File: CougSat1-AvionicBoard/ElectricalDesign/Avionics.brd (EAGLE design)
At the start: 90.4 x 95.8 mm, 213 parts, among them J1 +X Panel GPS, J10 iFJR SD1, J11 -Y, J12 +Z, J13 +X, J14 -Z, J15 +Y, J16 IFJR SD0, J2 IHU SD1, J3 SWD, J4 CougSat Card, J5 -X, J6 IHU SD0, J8 SWD, J9 SWD, U1 STM32L476RGT, U10 BNO055, U11 M24M01, U12 TXS0102DQM, U13 TXS0102DQM, U14 AD8515, U15 BNO055, U16 BNO055, U17 TXS0102DQM, U18 TXS0102DQM, U19 AD8515, U2 STM32L476RGT, U20 INA199C2, U21 INA199C2, U22 TXS0102DQM, U23 TXS0102DQM, U24 AD8515, U25 AD7291, U26 AD7291, U27 TXS0102DQM, U28 INA199C2, U29 AD8515, U3 STM32L476RGT, U30 DRV8837, U4 M24M01, U5 TXS0102DQM, U6 DRV8837, U7 DRV8837, U8 AD7291, U9 Venus838FLPx-L, Y1 8MHz ±10ppm, Y10 32.768kHz ±10ppm, Y2 32.768kHz ±10ppm, Y3 8MHz ±10ppm, Y4 32.768kHz ±10ppm, Y5 8MHz ±10ppm, Y6 32.768kHz ±10ppm, Y7 32.768kHz ±10ppm, Y8 32.768kHz ±10ppm

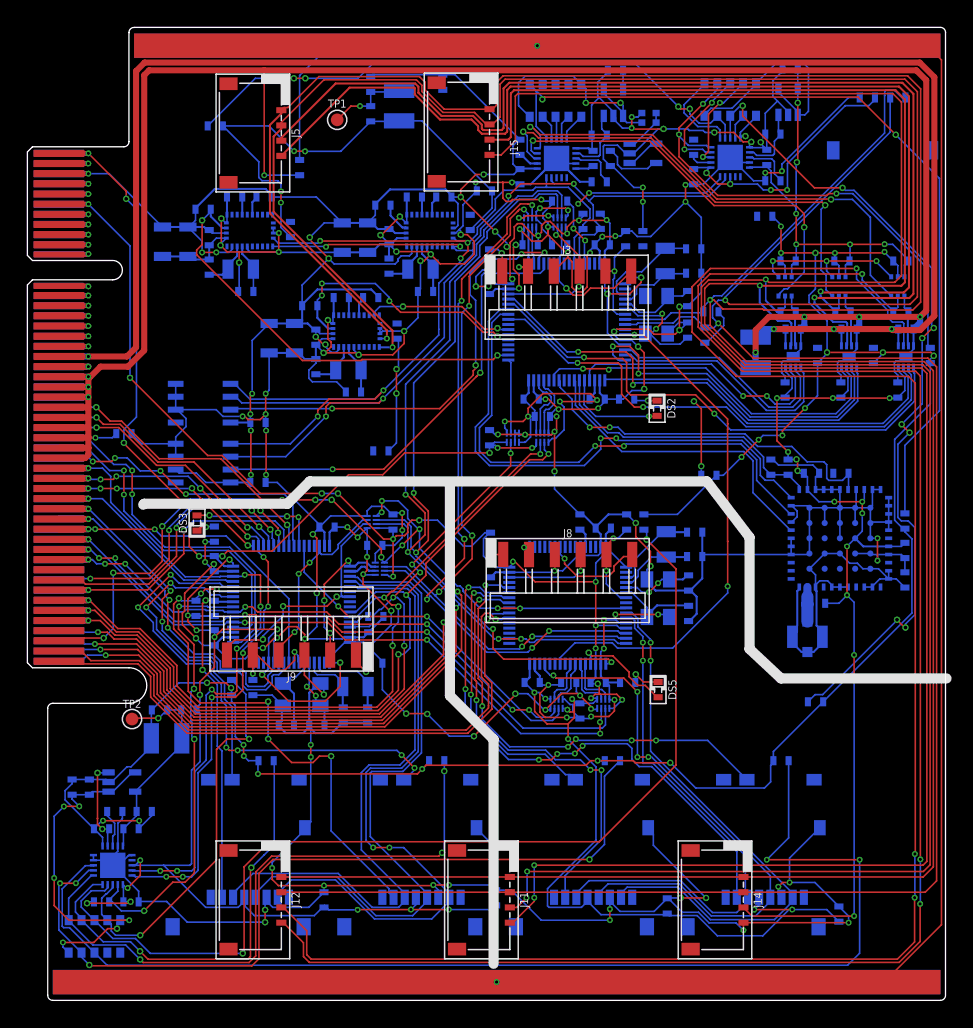
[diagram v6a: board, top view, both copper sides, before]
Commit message: Adjusted silkscreen and poured polygons
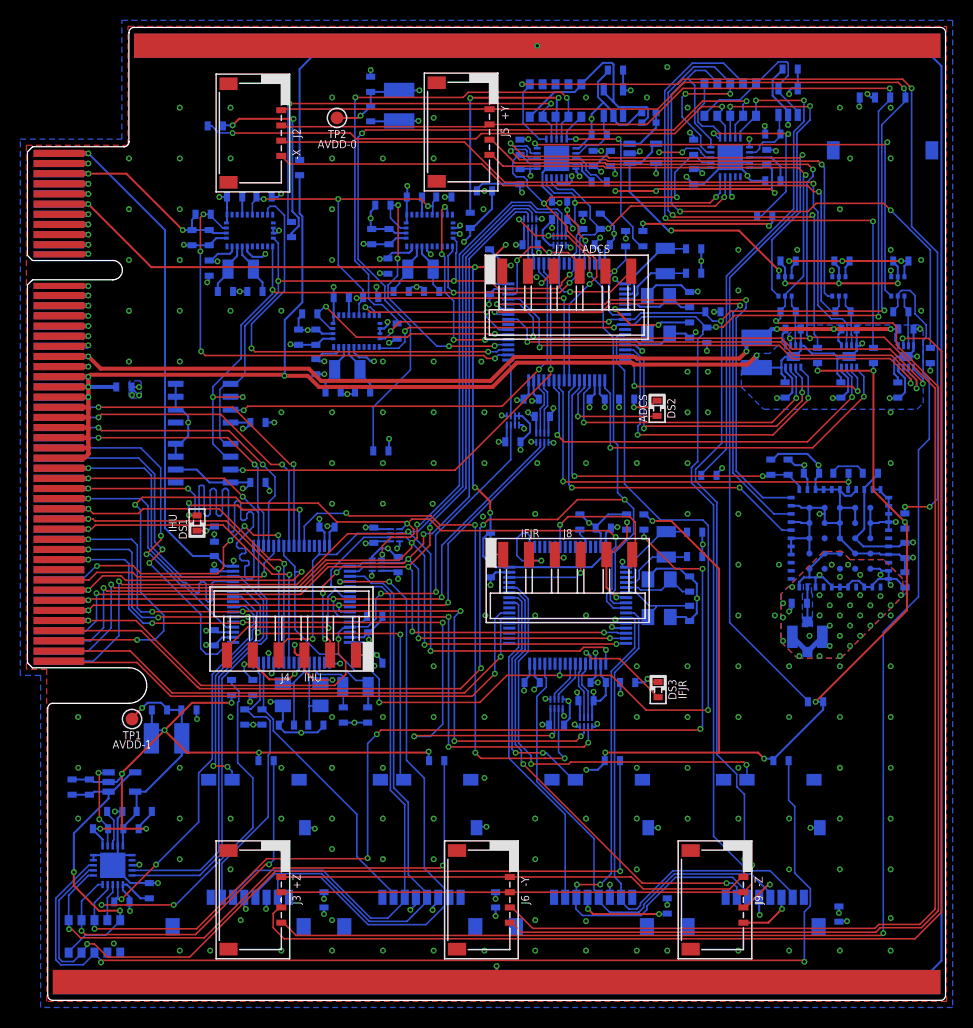
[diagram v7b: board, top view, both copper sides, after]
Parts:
- removed C100, C101, C102, C96, C99: 100nF 10%, CougsInSpace-Capacitors:1608
- removed DS5: Green, CougsInSpace-LEDs:1608-POL
- removed J16: IFJR SD0, CougsInSpace-Connectors:µSD-PUSH-PUSH
- removed R37, R38, R42: 1kΩ 0.1%, CougsInSpace-Resistors:1608
- removed R39, R41, R43, R44: 10kΩ 0.1%, CougsInSpace-Resistors:1608
- removed R45: 0Ω <20mΩ, CougsInSpace-Resistors:1608
- removed RN18: 10kΩ 5%, CougsInSpace-Resistors:3264
- removed Y10: 32.768kHz ±10ppm, CougsInSpace-Clocks:SMD-3215
- added C44, C50, C51, C67: 100nF 10%, CougsInSpace-Capacitors:1608
- added C68: 10pF 5%, CougsInSpace-Capacitors:1608
- added DS4: Green, CougsInSpace-LEDs:1608-POL
- added J7: SWD, CougsInSpace-Connectors:SMD2.54-1X06-R
- added R11, R15, R33, R8: 0Ω <20mΩ, CougsInSpace-Resistors:1608
- added R14, R18, R28, R9: 10kΩ 0.1%, CougsInSpace-Resistors:1608
- added RN4: 10kΩ 5%, CougsInSpace-Resistors:3264
- added Y9: 32.768kHz ±10ppm, CougsInSpace-Clocks:SMD-3215
- C1, C16, C58: value 10pF 5% -> 100nF 10%
- C10, C88, C89, C90: value 1µF 10% -> 100nF 10%
- C12, C38: value 100nF 10% -> 6.8nF 5%
- C13, C14, C23, C26, C27, C36, C37, C42: value 15pF 1% -> 100nF 10%
- C15, C30, C31, C32, C43, C72, C73, C75, C76: value 100nF 10% -> 15pF 1%
- C17: value 15pF 1% -> 10nF 10%
- C19, C22: value 10nF 10% -> 100nF 10%
- C2, C59: value 10pF 5% -> 1µF 10%
- C21, C25, C70, C71: value 100nF 10% -> 10pF 5%
- C24: value 15pF 1% -> 6.8nF 5%
- C3: value 10nF 10% -> 10µF 10%
- C33, C39, C45, C5, C6: device CougsInSpace-Capacitors:3216 -> CougsInSpace-Capacitors:1608
- C34, C64: value 10µF 10% -> 100nF 10%
- C35, C8: value 6.8nF 5% -> 100nF 10%
- C4, C79, C80: value 100nF 10% -> 1µF 10%
- C40: value 100nF 10% -> 4.7µF 10%; device CougsInSpace-Capacitors:3216 -> CougsInSpace-Capacitors:4028-POL
- C41: value 6.8nF 5% -> 15pF 1%
- C60, C81: value 100nF 10% -> 10µF 10%
- C65: value 100nF 10% -> 10nF 10%
- C66: value 10µF 10% -> 10nF 10%
- C69: value 1µF 10% -> 10pF 5%
- C77: value 100nF 10% -> 47µF; device CougsInSpace-Capacitors:1608 -> CougsInSpace-Capacitors:4028-POL
- C78: value 47µF -> 100nF 10%; device CougsInSpace-Capacitors:4028-POL -> CougsInSpace-Capacitors:1608
- C9: value 10pF 5% -> 4.7µF 10%; device CougsInSpace-Capacitors:1608 -> CougsInSpace-Capacitors:4028-POL
- C91, C93: value 4.7µF 10% -> 100nF 10%; device CougsInSpace-Capacitors:4028-POL -> CougsInSpace-Capacitors:1608
- DS1: value Green -> Yellow
- DS3: value Yellow -> Green
- J1: value +X Panel GPS -> CougSat Card; device CougsInSpace-Connectors:U.FL -> CougsInSpace-Boards:CARD-FULL
- J10: value iFJR SD1 -> IHU SD0
- J11: value -Y -> IHU SD1; device CougsInSpace-Connectors:PICOLOCK1.5-04 -> CougsInSpace-Connectors:µSD-PUSH-PUSH
- J12: value +Z -> IFJR SD0; device CougsInSpace-Connectors:PICOLOCK1.5-04 -> CougsInSpace-Connectors:µSD-PUSH-PUSH
- J13: value +X -> iFJR SD1; device CougsInSpace-Connectors:PICOLOCK1.5-04 -> CougsInSpace-Connectors:µSD-PUSH-PUSH
- J14: value -Z -> +X Panel GPS; device CougsInSpace-Connectors:PICOLOCK1.5-04 -> CougsInSpace-Connectors:U.FL
- J15: value +Y -> +X
- J2: value IHU SD1 -> -X; device CougsInSpace-Connectors:µSD-PUSH-PUSH -> CougsInSpace-Connectors:PICOLOCK1.5-04
- J3: value SWD -> +Z; device CougsInSpace-Connectors:SMD2.54-1X06-R -> CougsInSpace-Connectors:PICOLOCK1.5-04
- J4: value CougSat Card -> SWD; device CougsInSpace-Boards:CARD-FULL -> CougsInSpace-Connectors:SMD2.54-1X06-R
- J5: value -X -> +Y
- J6: value IHU SD0 -> -Y; device CougsInSpace-Connectors:µSD-PUSH-PUSH -> CougsInSpace-Connectors:PICOLOCK1.5-04
- J9: value SWD -> -Z; device CougsInSpace-Connectors:SMD2.54-1X06-R -> CougsInSpace-Connectors:PICOLOCK1.5-04
- R1, R3, R5: value 0Ω <20mΩ -> 10kΩ 0.1%
- R12, R17: value 10kΩ 0.1% -> 1kΩ 0.1%
- R13: value 1kΩ 0.1% -> 10kΩ 0.1%
- R19: value 1kΩ 0.1% -> 0Ω <20mΩ
- R20: value 10kΩ 0.1% -> 0Ω <20mΩ
- R23, R4: value 0Ω <20mΩ -> 1kΩ 0.1%
- R30: value 50mΩ 1% -> 1kΩ 0.1%
- R32: value 10kΩ 0.1% -> 50mΩ 1%
- RN1: value 20kΩ 0.1% -> 10kΩ 5%; device CougsInSpace-Resistors:1616 -> CougsInSpace-Resistors:3264
- RN3: value 10kΩ 5% -> 20kΩ 0.1%; device CougsInSpace-Resistors:3264 -> CougsInSpace-Resistors:1616
- U1: value STM32L476RGT -> AD7291; device CougsInSpace-IC-µController:QFP-64-1010 -> CougsInSpace-IC-Conversion:QFN-20-4040
- U11: value M24M01 -> TXS0102DQM; device CougsInSpace-IC-Memory:SO8 -> CougsInSpace-IC-Comms:X2SON-8
- U14, U19: value AD8515 -> TXS0102DQM; device CougsInSpace-IC-Amplifiers:SOT23-5 -> CougsInSpace-IC-Comms:X2SON-8
- U15: value BNO055 -> AD7291; device CougsInSpace-Sensors:LGA-28-4050 -> CougsInSpace-IC-Conversion:QFN-20-4040
- U16: value BNO055 -> TXS0102DQM; device CougsInSpace-Sensors:LGA-28-4050 -> CougsInSpace-IC-Comms:X2SON-8
- U17, U18: value TXS0102DQM -> STM32L476RGT; device CougsInSpace-IC-Comms:X2SON-8 -> CougsInSpace-IC-µController:QFP-64-1010
- U2: value STM32L476RGT -> AD8515; device CougsInSpace-IC-µController:QFP-64-1010 -> CougsInSpace-IC-Amplifiers:SOT23-5
- U20, U21: value INA199C2 -> AD8515; device CougsInSpace-IC-Amplifiers:SOT363 -> CougsInSpace-IC-Amplifiers:SOT23-5
- U22: value TXS0102DQM -> AD7291; device CougsInSpace-IC-Comms:X2SON-8 -> CougsInSpace-IC-Conversion:QFN-20-4040
- U23: value TXS0102DQM -> INA199C2; device CougsInSpace-IC-Comms:X2SON-8 -> CougsInSpace-IC-Amplifiers:SOT363
- U25: value AD7291 -> DRV8837; device CougsInSpace-IC-Conversion:QFN-20-4040 -> CougsInSpace-IC-Other:WSON-8
- U26: value AD7291 -> INA199C2; device CougsInSpace-IC-Conversion:QFN-20-4040 -> CougsInSpace-IC-Amplifiers:SOT363
- U27: value TXS0102DQM -> Venus838FLPx-L; device CougsInSpace-IC-Comms:X2SON-8 -> CougsInSpace-RF:VENUS-1010
- U28: value INA199C2 -> DRV8837; device CougsInSpace-IC-Amplifiers:SOT363 -> CougsInSpace-IC-Other:WSON-8
- U29: value AD8515 -> INA199C2; device CougsInSpace-IC-Amplifiers:SOT23-5 -> CougsInSpace-IC-Amplifiers:SOT363
- U3: value STM32L476RGT -> M24M01; device CougsInSpace-IC-µController:QFP-64-1010 -> CougsInSpace-IC-Memory:SO8
- U5: value TXS0102DQM -> BNO055; device CougsInSpace-IC-Comms:X2SON-8 -> CougsInSpace-Sensors:LGA-28-4050
- U6: value DRV8837 -> STM32L476RGT; device CougsInSpace-IC-Other:WSON-8 -> CougsInSpace-IC-µController:QFP-64-1010
- U7: value DRV8837 -> BNO055; device CougsInSpace-IC-Other:WSON-8 -> CougsInSpace-Sensors:LGA-28-4050
- U8: value AD7291 -> TXS0102DQM; device CougsInSpace-IC-Conversion:QFN-20-4040 -> CougsInSpace-IC-Comms:X2SON-8
- U9: value Venus838FLPx-L -> TXS0102DQM; device CougsInSpace-RF:VENUS-1010 -> CougsInSpace-IC-Comms:X2SON-8
- Y1, Y3, Y5: value 8MHz ±10ppm -> 32.768kHz ±10ppm; device CougsInSpace-Clocks:SMD-5032 -> CougsInSpace-Clocks:SMD-3215
- Y2, Y6, Y7: value 32.768kHz ±10ppm -> 8MHz ±10ppm; device CougsInSpace-Clocks:SMD-3215 -> CougsInSpace-Clocks:SMD-5032
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- renumbered C95 to C52, R36 to R16, R40 to R10, R46 to R24
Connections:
- net !ADCS_ADC_RESET!: now also R18.1, R25.1, U15.17, U17.24, U22.17; no longer R17.1, R6.1, U2.24, U25.17, U8.17
- net !C&DH_ADC_RESET: now also R1.1, U1.17, U6.24; no longer R7.1, U26.17, U3.24
- net !GPS_RESET: now also C79.1, R28.1, U17.22, U27.1; no longer C10.1, R12.1, U2.22, U9.1
- net !IMU0_BOOT_A: now also R3.1, U17.34, U5.4; no longer R43.1, U10.4, U2.34
- net !IMU1_BOOT_A: now also R13.1, U10.4, U17.36; no longer R39.1, U15.4, U2.36
- net !IMU2_BOOT_A: now also R9.2, U17.38, U7.4; no longer R41.2, U16.4, U2.38
- net !IMU_RESET: now also R14.1, R7.1, U17.25, U5.11, U7.11; no longer R20.1, R32.1, U15.11, U16.11, U2.25
- net 3.3V_0: now also C13.1, C14.1, C26.1, C27.1, C33.1, C36.1, C46.1, C47.1, C53.1, C7.1, FB1.1, J1.A1, J1.B1, J10.VDD, J11.VDD, R1.2, R12.2, R5.2, R6.2, U1.13, U1.16, U11.8, U13.8, U14.8, U19.8, U6.1, U6.13, U6.19, U6.32, U6.48, U6.64, U8.1, U9.1; no longer C101.1, C15.1, C25.1, C60.1, C61.1, C62.1, C63.1, C83.1, C96.1, C99.1, FB2.1, J2.VDD, J4.A1, J4.B1, J6.VDD, R25.2, R38.2, R44.2, R7.2, U17.1, U18.1, U22.8, U23.8, U26.13, U26.16, U27.8, U3.1, U3.13, U3.19, U3.32, U3.48, U3.64, U5.8
- net 3.3V_2: now also C10.1, C19.1, C22.1, C23.1, C24.1, C37.1, C38.1, C44.1, C50.1, C57.1, C61.1, C82.1, C86.1, C88.1, C91.1, C93.1, DS4.A, FB2.1, J1.A3, J1.B3, J15.3, J9.3, R13.2, R14.2, R18.2, R25.2, R27.2, R28.2, R3.2, R7.2, R9.1, U10.17, U11.1, U11.5, U13.5, U15.11, U15.13, U15.16, U16.1, U17.1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; no longer C29.1, C33.1, C39.1, C40.1, C41.1, C45.1, C46.1, C47.1, C5.1, C6.1, C7.1, C72.1, C76.1, C79.1, C8.1, C81.1, DS1.A, FB1.1, J13.3, J14.3, J4.A3, J4.B3, R12.2, R17.2, R19.2, R20.2, R32.2, R39.2, R41.1, R43.2, R6.2, U11.2, U11.8, U15.17, U15.28, U15.3, U16.28, U16.3, U2.1, U2.13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
- net 3.3V_5: now also C39.1, C45.1, C51.1, C58.1, C62.1, C67.1, C87.1, J1.A6, J1.B6, J12.VDD, J13.VDD, R17.2, U14.1, U14.5, U16.8, U18.1, U18.13, U18.19, U18.32, U18.48, U18.64, U19.1, U19.5, U8.8, U9.8; no longer C100.1, C102.1, C21.1, C30.1, C31.1, C56.1, C57.1, J10.VDD, J16.VDD, J4.A6, J4.B6, R37.2, U1.1, U1.13, U1.19, U1.32, U1.48, U1.64, U13.8, U17.8, U18.8, U23.1, U23.5, U27.1, U27.5
- net ADCS_!NRST: now also C65.1, J7.5, U17.7; no longer C3.1, J3.5, U2.7
- net ADCS_ADC0_DCAP: now also C59.1, U15.8; no longer C89.1, U8.8
- net ADCS_ADC0_VREF: now also C60.1, U15.7, U20.3; no longer C34.1, U14.3, U8.7
- net ADCS_ADC1_DCAP: now also C80.1, U22.8; no longer C90.1, U25.8
- net ADCS_ADC1_VREF: now also C81.1, U22.7, U24.3; no longer C66.1, U19.3, U25.7
- net ADCS_BOOT0: now also R19.2, U17.60; no longer R5.2, U2.60
- net ADCS_BUS_IRQ: now also U11.2, U17.33; no longer U2.33, U22.2
- net ADCS_BUS_SCL: now also U13.3, U17.29; no longer U2.29, U5.3
- net ADCS_BUS_SDA: now also U13.2, U17.30; no longer U2.30, U5.2
- net ADCS_HALF_REF: now also U21.4, U23.1, U26.1, U29.1; no longer U20.1, U24.1, U24.4, U28.1
- net ADCS_HALF_REF_UNBUFF: now also RN3.1, RN3.2, U21.3; no longer RN1.1, RN1.2, U24.3
- net ADCS_I2C0_SCL: now also R21.1, U15.15, U17.58, U22.15, U3.5, U5.19; no longer R26.1, U11.5, U15.19, U2.58, U25.15, U8.15
- net ADCS_I2C0_SDA: now also U15.14, U17.59, U22.14, U3.6, U5.20; no longer U11.6, U15.20, U2.59, U25.14, U8.14
- net ADCS_I2C1_SCL: now also J2.1, J3.1, J6.1, J9.1, R27.1, U17.8, U7.19; no longer J11.1, J12.1, J13.1, J14.1, R21.1, U16.19, U2.8
- net ADCS_I2C1_SDA: now also J2.2, J3.2, J6.2, J9.2, R26.1, U17.9, U7.20; no longer J11.2, J12.2, J13.2, J14.2, R19.1, U16.20, U2.9
- net ADCS_IMU1_OSC_32_IN: now also C41.1, U10.27, Y5.2; no longer C37.1, U15.27, Y10.2
- net ADCS_IMU1_OSC_32_IN1: now also C15.1, U5.27, Y1.2; no longer C27.1, U10.27, Y7.2
- net ADCS_IMU1_OSC_32_IN2: now also C28.1, U7.27, Y3.2; no longer C42.1, U16.27, Y8.2
- net ADCS_IMU1_OSC_32_OUT: now also C43.1, U10.26, Y5.1; no longer C36.1, U15.26, Y10.1
- net ADCS_IMU1_OSC_32_OUT1: now also C18.1, U5.26, Y1.1; no longer C26.1, U10.26, Y7.1
- net ADCS_IMU1_OSC_32_OUT2: now also C31.1, U7.26, Y3.1; no longer C28.1, U16.26, Y8.1
- net ADCS_JTCK: now also J7.2, U17.49; no longer J3.2, U2.49
- net ADCS_JTDI: now also U17.50; no longer U2.50
- net ADCS_JTDO: now also J7.6, U16.2, U17.55; no longer J3.6, U13.2, U2.55
- net ADCS_JTMS: now also J7.4, U16.3, U17.46; no longer J3.4, U13.3, U2.46
- net ADCS_LED: now also U17.21; no longer U2.21
- net ADCS_LED_GND: now also R23.1; no longer R42.1
- net ADCS_OSC_32_IN: now also C72.1, U17.4, Y8.1; no longer C14.1, U2.4, Y2.1
- net ADCS_OSC_32_OUT: now also C73.1, U17.3, Y8.2; no longer C13.1, U2.3, Y2.2
- net ADCS_OSC_IN: now also C71.1, U17.5, Y6.1; no longer C1.1, U2.5, Y5.1
- net ADCS_OSC_OUT: now also C70.1, U17.6, Y6.3; no longer C2.1, U2.6, Y5.3
- net ADCS_SWD_VSENCE: now also J7.1; no longer J3.1
- net AGND: now also C1.2, C2.2, C3.2, C40.C, C5.2, C56.2, C6.2, C60.2, C63.2, C78.2, C8.2, C81.2, C83.2, C89.2, C9.C, R15.1, RN3.4, U1.6, U15.6, U2.2, U22.6, U23.2, U26.2; no longer C43.2, C53.2, C65.2, C66.2, C69.2, C70.2, C71.2, C80.2, C82.2, C85.2, C86.2, C87.2, C91.C, C93.C, C94.2, R2.1, RN1.4, U14.2, U19.2, U25.6, U26.6, U28.2, U8.6
- net AVDD-0: now also C34.1, C40.A, C56.1, C63.1, C64.1, C78.1, C83.1, C84.1, C89.1, FB2.2, TP2.1, U15.10, U20.5, U21.5, U22.10, U23.3, U26.3, U29.3; no longer C43.1, C53.1, C71.1, C80.1, C82.1, C85.1, C86.1, C87.1, C91.A, FB1.2, TP1.1, U14.5, U19.5, U20.3, U21.3, U25.10, U28.3, U8.10
- net AVDD-1: now also C5.1, C6.1, C8.1, C9.A, FB1.2, TP1.1, U1.10, U2.5; no longer C65.1, C84.1, C93.A, C94.1, FB2.2, TP2.1, U26.10, U29.5
- net AVREF-0: now also RN2.10, RN2.5, RN3.3, U20.1, U20.4; no longer RN1.3, RN18.10, RN18.5, U14.1, U14.4
- net AVREF-1: now also RN4.10, RN4.5, U24.1, U24.4; no longer RN2.10, RN2.5, U19.1, U19.4
- net AVREF-2: now also C1.1, C2.1, RN1.10, RN1.5, U2.1, U2.4; no longer C69.1, C70.1, RN3.10, RN3.5, U29.1, U29.4
- net BUS_I2C0_IRQ: now also J1.A45, J1.B45, U11.7, U6.61; no longer J4.A45, J4.B45, U22.7, U3.61
- net BUS_I2C0_SCL: now also J1.A44, J1.B44, U13.6, U6.58; no longer J4.A44, J4.B44, U3.58, U5.6
- net BUS_I2C0_SDA: now also J1.A43, J1.B43, U13.7, U6.59; no longer J4.A43, J4.B43, U3.59, U5.7
- net BUS_I2C1_IRQ: now also J1.A32, J1.B32, U6.33; no longer J4.A32, J4.B32, U3.33
- net BUS_I2C1_SCL: now also J1.A31, J1.B31, U1.15, U6.34; no longer J4.A31, J4.B31, U26.15, U3.34
- net BUS_I2C1_SDA: now also J1.A30, J1.B30, U1.14, U6.30; no longer J4.A30, J4.B30, U26.14, U3.30
- net BUS_JTAG_TCK: now also J1.A46, U18.14, U8.7; no longer J4.A46, U1.14, U17.7
- net BUS_JTAG_TDI: now also J1.A47, U18.15, U8.6; no longer J4.A47, U1.15, U17.6
- net BUS_JTAG_TDO: now also J1.A48, U16.7, U18.16, U9.7; no longer J4.A48, U1.16, U13.7, U18.7
- net BUS_JTAG_TMS: now also J1.A49, U16.6, U18.17, U9.6; no longer J4.A49, U1.17, U13.6, U18.6
- net BUS_SPI_IFJR_CS: now also U14.6, U6.43; no longer U27.6, U3.43
- net BUS_SPI_MISO: now also J1.A38, J1.B38, U19.6, U6.22; no longer J4.A38, J4.B38, U23.6, U3.22
- net BUS_SPI_MOSI: now also J1.A39, J1.B39, U14.7, U6.21; no longer J4.A39, J4.B39, U27.7, U3.23
- net BUS_SPI_SCK: now also J1.A37, J1.B37, U19.7, U6.23; no longer J4.A37, J4.B37, U23.7, U3.21
- net C&DH_ADC_DCAP: now also C4.1, U1.8; no longer C88.1, U26.8
- net C&DH_ADC_VREF: now also C3.1, U1.7, U2.3; no longer C64.1, U26.7, U29.3
- net CHASSIS: now also J1.CHASSIS@1, J1.CHASSIS@2, J1.CHASSIS@3, J1.CHASSIS@4, R8.1; no longer J4.CHASSIS@1, J4.CHASSIS@2, J4.CHASSIS@3, J4.CHASSIS@4, R3.1
- net COIL-X_!SLEEP: now also U17.27, U28.7; no longer U2.27, U30.7
- net COIL-X_COIL+: now also J2.3, U28.2; no longer J5.3, U30.2
- net COIL-X_COIL-: now also J2.4, R31.2, U26.5; no longer J5.4, R29.2, U20.5
- net COIL-X_CURRENT: now also U15.18, U26.6; no longer U20.6, U8.18
- net COIL-X_IN1: now also U17.16, U28.6; no longer U2.16, U30.6
- net COIL-X_IN2: now also U17.17, U28.5; no longer U2.17, U30.5
- net COIL-X_OUT2: now also R31.1, U26.4, U28.3; no longer R29.1, U20.4, U30.3
- net COIL-Y_!SLEEP: now also U17.20, U25.7; no longer U2.20, U6.7
- net COIL-Y_COIL+: now also J5.3, J6.3, U25.2; no longer J11.3, J15.3, U6.2
- net COIL-Y_COIL-: now also J5.4, J6.4, R29.2, U23.5; no longer J11.4, J15.4, R30.2, U21.5
- net COIL-Y_CURRENT: now also U15.19, U23.6; no longer U21.6, U8.19
- net COIL-Y_IN1: now also U17.14, U25.6; no longer U2.14, U6.6
- net COIL-Y_IN2: now also U17.15, U25.5; no longer U2.15, U6.5
- net COIL-Y_OUT2: now also R29.1, U23.4, U25.3; no longer R30.1, U21.4, U6.3
- net COIL-Z_!SLEEP: now also U17.45, U30.7; no longer U2.45, U7.7
- net COIL-Z_COIL+: now also J3.3, U30.2; no longer J12.3, U7.2
- net COIL-Z_COIL-: now also J3.4, R32.2, U29.5; no longer J12.4, R31.2, U28.5
- net COIL-Z_CURRENT: now also U15.20, U29.6; no longer U28.6, U8.20
- net COIL-Z_IN1: now also U17.41, U30.6; no longer U2.41, U7.6
- net COIL-Z_IN2: now also U17.44, U30.5; no longer U2.44, U7.5
- net COIL-Z_OUT2: now also R32.1, U29.4, U30.3; no longer R31.1, U28.4, U7.3
- net COM_SPI_CS: now also J1.A36, J1.B36, U6.9; no longer J4.A36, J4.B36, U3.9
- net COM_SPI_MISO: now also J1.A34, J1.B34, U6.10; no longer J4.A34, J4.B34, U3.10
- net COM_SPI_MOSI: now also J1.A35, J1.B35, U6.11; no longer J4.A35, J4.B35, U3.11
- net COM_SPI_SCK: now also J1.A33, J1.B33, U6.29; no longer J4.A33, J4.B33, U3.29
- net CTRL_SYNC: now also J1.A42, J1.B42, U17.11, U18.26, U6.39; no longer J4.A42, J4.B42, U1.26, U2.11, U3.39
- net DGND: now also C16.1, C29.1, C32.2, C38.2, C4.2, C42.1, C43.2, C44.2, C50.2, C51.2, C53.2, C65.2, C66.2, C67.2, C68.2, C69.2, C70.2, C71.2, C72.2, C73.2, C74.2, C75.2, C76.2, C80.2, C86.2, C87.2, C93.2, J11.SW-LEVER, J11.VSS, J12.SW-LEVER, J12.VSS, J13.SW-LEVER, J13.VSS, J15.4, J4.3, J7.3, J9.4, R11.1, R15.2, R19.1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; no longer C1.2, C100.2, C101.2, C102.2, C16.2, C2.2, C29.2, C3.2, C32.1, C38.1, C4.1, C40.2, C42.2, C5.2, C56.2, C6.2, C60.2, C63.2, C8.2, C81.2, C83.2, C88.2, C89.2, C9.2, C90.2, C96.2, C99.2, J13.4, J14.4, J16.SW-LEVER, J16.VSS, J2.SW-LEVER, J2.VSS, J3.3, J6.SW-LEVER, J6.VSS, J9.3, R1.2, R23.1, R27.2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
- net EEPROM0_WC: now also U17.51; no longer U2.51
- net EEPROM1_WC: now also U17.52, U3.7; no longer U11.7, U2.52
- net GPS_LED: now also R30.1, U17.26, U27.7; no longer R13.1, U2.26, U9.7
- net GPS_LED_DIODE: now also DS4.C, R30.2; no longer DS1.C, R13.2
- net GPS_PULSE: now also U17.23, U27.40; no longer U2.23, U9.40
- net GPS_RFIN: now also J14.CENTER, U27.32; no longer J1.CENTER, U9.32
- net GPS_RX: now also U17.43, U27.44; no longer U2.43, U9.44
- net GPS_TX: now also U17.42, U27.42; no longer U2.42, U9.42
- net IFJR_!NRST: now also C66.1, U18.7; no longer C19.1, U1.7
- net IFJR_BOOT0: now also R20.2, U18.60; no longer R23.2, U1.60
- net IFJR_BUS_CS: now also U14.2, U18.24; no longer U1.24, U27.2
- net IFJR_BUS_MISO: now also U18.22, U19.2; no longer U1.22, U23.2
- net IFJR_BUS_MOSI: now also U14.3, U18.23; no longer U1.23, U27.3
- net IFJR_BUS_SCK: now also U18.21, U19.3; no longer U1.21, U23.3
- net IFJR_JTCK: now also U18.49; no longer U1.49
- net IFJR_JTDO: now also U18.55; no longer U1.55
- net IFJR_JTMS: now also U18.46; no longer U1.46
- net IFJR_LED: now also DS3.A, U18.20; no longer DS5.A, U1.20
- net IFJR_LED_GND: now also DS3.C; no longer DS5.C
- net IFJR_OSC_32_IN: now also C76.1, U18.4, Y9.1; no longer C18.1, U1.4, Y4.1
- net IFJR_OSC_32_OUT: now also C75.1, U18.3, Y9.2; no longer C17.1, U1.3, Y4.2
- net IFJR_OSC_IN: now also C68.1, U18.5, Y7.1; no longer C9.1, U1.5, Y1.1
- net IFJR_OSC_OUT: now also C69.1, U18.6, Y7.3; no longer C16.1, U1.6, Y1.3
- net IFJR_SD_CS0: now also J12.CD/DAT3, U18.41; no longer J16.CD/DAT3, U1.41
- net IFJR_SD_CS1: now also J13.CD/DAT3, U18.43; no longer J10.CD/DAT3, U1.43
- net IFJR_SD_SW0: now also J12.SW, U18.42; no longer J16.SW, U1.42
- net IFJR_SD_SW1: now also J13.SW, U18.44; no longer J10.SW, U1.44
- net IFJR_SPI_MISO: now also J12.DAT0, J13.DAT0, U18.10; no longer J10.DAT0, J16.DAT0, U1.10
- net IFJR_SPI_MOSI: now also J12.CMD, J13.CMD, U18.11; no longer J10.CMD, J16.CMD, U1.11
- net IFJR_SPI_SCK: now also J12.CLK, J13.CLK, U18.29; no longer J10.CLK, J16.CLK, U1.29
- net IFJR_SWD_VSENSE: now also R17.1; no longer R37.1
- net IHU_!NRST: now also C17.1, J4.5, U6.7; no longer C22.1, J9.5, U3.7
- net IHU_BOOT0: now also R11.2, U6.60; no longer R45.2, U3.60
- net IHU_GPIO-0: now also J1.A24, U6.41; no longer J4.A24, U3.40
- net IHU_GPIO-1: now also J1.A25, U6.40; no longer J4.A25, U3.36
- net IHU_GPIO-2: now also J1.A26, U6.36; no longer J4.A26, U3.35
- net IHU_GPIO-3: now also J1.A27, U6.35; no longer J4.A27, U3.17
- net IHU_GPIO-4: now also J1.A28, U6.20; no longer J4.A28, U3.20
- net IHU_GPIO-5: now also J1.A29, U6.17; no longer J4.A29, U3.41
- net IHU_GPIO-6: now also J1.A41, U6.38; no longer J4.A41, U3.38
- net IHU_GPIO-7: now also J1.B41, U6.37; no longer J4.B41, U3.37
- net IHU_JTCK: now also J4.2, U6.49, U8.3; no longer J9.2, U17.3, U3.49
- net IHU_JTDI: now also U6.50, U8.2; no longer U17.2, U3.50
- net IHU_JTDO: now also J4.6, U6.55, U9.2; no longer J9.6, U18.2, U3.55
- net IHU_JTMS: now also J4.4, U6.46, U9.3; no longer J9.4, U18.3, U3.46
- net IHU_LED: now also DS1.A, U6.42; no longer DS3.A, U3.42
- net IHU_LED_GND: now also DS1.C, R4.1; no longer DS3.C, R27.1
- net IHU_OSC_32_IN: now also C30.1, U6.4, Y4.1; no longer C24.1, U3.4, Y6.1
- net IHU_OSC_32_OUT: now also C32.1, U6.3, Y4.2; no longer C23.1, U3.3, Y6.2
- net IHU_OSC_IN: now also C25.1, U6.5, Y2.1; no longer C58.1, U3.5, Y3.1
- net IHU_OSC_OUT: now also C21.1, U6.6, Y2.3; no longer C59.1, U3.6, Y3.3
- net IHU_SD_CS0: now also J10.CD/DAT3, R5.1, U6.15; no longer J6.CD/DAT3, R25.1, U3.25
- net IHU_SD_CS1: now also J11.CD/DAT3, R6.1, U6.14; no longer J2.CD/DAT3, R44.1, U3.27
- net IHU_SD_SW0: now also J10.SW, U6.26; no longer J6.SW, U3.26
- net IHU_SD_SW1: now also J11.SW, U6.28; no longer J2.SW, U3.28
- net IHU_SPI_MISO: now also J10.DAT0, J11.DAT0, U6.52; no longer J2.DAT0, J6.DAT0, U3.52
- net IHU_SPI_MOSI: now also J10.CMD, J11.CMD, U6.53; no longer J2.CMD, J6.CMD, U3.53
- net IHU_SPI_SCK: now also J10.CLK, J11.CLK, U6.51; no longer J2.CLK, J6.CLK, U3.51
- net IHU_SWD_VSENSE: now also J4.1, R12.1; no longer J9.1, R38.1
- net IMU0_CAP: now also C16.2, U5.9; no longer C4.2, U10.9
- net IMU0_INT: now also U17.35, U5.14; no longer U10.14, U2.35
- net IMU1_CAP: now also C42.2, U10.9; no longer C38.2, U15.9
- net IMU1_INT: now also U10.14, U17.37; no longer U15.14, U2.37
- net IMU2_CAP: now also C29.2, U7.9; no longer C32.2, U16.9
- net IMU2_INT: now also U17.39, U7.14; no longer U16.14, U2.39
- net JTAG_EN-2: now also J1.B48, U18.38; no longer J4.B48, U1.38
- net JTAG_EN-3: now also J1.B49, U18.39; no longer J4.B49, U1.39
- net JTAG_EN_ADCS: now also J1.B46, U16.5, U18.8; no longer J4.B46, U1.8, U13.5
- net JTAG_EN_IHU: now also J1.B47, U18.9, U8.5, U9.5; no longer J4.B47, U1.9, U17.5, U18.5
- net PGND: now also C77.C, C82.2, C85.2, C88.2, C90.2, C91.2, C94.2, J1.A21, J1.A22, J1.A23, J1.B21, J1.B22, J1.B23, J1.B24, J1.B25, J1.B26, J1.B27, J1.B28, J1.B29, R2.1, R8.2, U25.4, U25.PAD, U28.4, U28.PAD; no longer C72.2, C73.2, C74.2, C75.2, C76.2, C77.2, C78.C, J4.A21, J4.A22, J4.A23, J4.B21, J4.B22, J4.B23, J4.B24, J4.B25, J4.B26, J4.B27, J4.B28, J4.B29, R1.1, R3.2, U6.4, U6.PAD, U7.4, U7.PAD
- net PR_3.3V-1: now also J1.A2, J1.B2; no longer J4.A2, J4.B2
- net PR_3.3V-10: now also J1.A11, J1.B11; no longer J4.A11, J4.B11
- net PR_3.3V-11: now also J1.A12, J1.B12; no longer J4.A12, J4.B12
- net PR_3.3V-12: now also J1.A13, J1.B13; no longer J4.A13, J4.B13
- net PR_3.3V-3: now also J1.A4, J1.B4; no longer J4.A4, J4.B4
- net PR_3.3V-4: now also J1.A5, J1.B5; no longer J4.A5, J4.B5
- net PR_3.3V-6: now also J1.A7, J1.B7; no longer J4.A7, J4.B7
- net PR_3.3V-7: now also J1.A8, J1.B8; no longer J4.A8, J4.B8
- net PR_3.3V-8: now also J1.A9, J1.B9; no longer J4.A9, J4.B9
- net PR_3.3V-9: now also J1.A10, J1.B10; no longer J4.A10, J4.B10
- net PR_BATT-0: now also J1.A14, J1.B14; no longer J4.A14, J4.B14
- net PR_BATT-1: now also J1.A15, J1.B15; no longer J4.A15, J4.B15
- net PR_BATT-2: now also J1.A16, J1.B16; no longer J4.A16, J4.B16
- net PR_BATT-3: now also J1.A17, J1.B17; no longer J4.A17, J4.B17
- net PR_BATT-4: now also J1.A18, J1.B18; no longer J4.A18, J4.B18
- net PR_BATT-6: now also J1.A20, J1.B20; no longer J4.A20, J4.B20
- net RFGND: now also J14.SHIELD@1, J14.SHIELD@13, J14.SHIELD@2, R33.1, U27.21, U27.22, U27.24, U27.25, U27.27, U27.28, U27.29, U27.31, U27.33, U27.61, U27.62, U27.65, U27.69; no longer J1.SHIELD@1, J1.SHIELD@13, J1.SHIELD@2, R4.1, U9.21, U9.22, U9.24, U9.25, U9.27, U9.28, U9.29, U9.31, U9.33, U9.61, U9.62, U9.65, U9.69
- net TEMP_ADCS: now also RN2.1, RT10.2, U15.5; no longer RN18.1, RT15.2, U8.5
- net TEMP_GPS: now also RN2.6, RT18.2, U15.1; no longer RN18.6, RT1.2, U8.1
- net TEMP_H-BRIDGE-X: now also RN4.9, RT17.2, U22.18; no longer RN2.9, RT8.2, U25.18
- net TEMP_H-BRIDGE-Y: now also RN4.8, RT16.2, U22.19; no longer RN2.8, RT9.2, U25.19
- net TEMP_H-BRIDGE-Z: now also RN4.7, RT19.2, U22.20; no longer RN2.7, RT10.2, U25.20
- net TEMP_IFJR: now also RN1.8, RT11.2, U1.19; no longer RN3.8, RT3.2, U26.19
- net TEMP_IHU: now also RN1.9, RT2.2, U1.18; no longer RN3.9, RT5.2, U26.18
- net TEMP_IMU0: now also RN2.4, RT4.2, U15.2; no longer RN18.4, RT16.2, U8.2
- net TEMP_IMU1: now also RN2.3, RT8.2, U15.3; no longer RN18.3, RT17.2, U8.3
- net TEMP_IMU2: now also RN2.2, RT6.2, U15.4; no longer RN18.2, RT18.2, U8.4
- net TEMP_PCB-0: now also RN4.6, RT13.2, U22.1; no longer RN2.6, RT11.2, U25.1
- net TEMP_PCB-1: now also RN4.4, RT1.2, U22.2; no longer RN2.4, RT12.2, U25.2
- net TEMP_PCB-2: now also RN4.3, RT15.2, U22.3; no longer RN2.3, RT13.2, U25.3
- net TEMP_PCB-3: now also RN4.2, RT5.2, U22.4; no longer RN2.2, RT14.2, U25.4
- net TEMP_PCB-4: now also RN4.1, RT12.2, U22.5; no longer RN2.1, RT19.2, U25.5
- net TEMP_SD_IFJR0: now also RN1.4, RT9.2, U1.2; no longer RN3.4, RT2.2, U26.2
- net TEMP_SD_IFJR1: now also RN1.3, RT14.2, U1.3; no longer RN3.3, RT4.2, U26.3
- net TEMP_SD_IHU0: now also RN1.7, RT3.2, U1.20; no longer RN3.7, RT6.2, U26.20
- net TEMP_SD_IHU1: now also RN1.6, U1.1; no longer RN3.6, U26.1
- net VBATT_5: now also C77.A, C85.1, C90.1, C94.1, J1.A19, J1.B19, U25.1, U28.1; no longer C73.1, C75.1, C77.1, C78.A, J4.A19, J4.B19, U6.1, U7.1
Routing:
- net DGND: track 740.7 -> 1498.7 mm, vias 89 -> 237
- net JTAG_EN_ADCS: track 4.10 -> 121.7 mm, vias 2 -> 6
- net ADCS_I2C1_SCL: track 320.0 -> 241.9 mm, vias 2 -> 6
- net ADCS_I2C1_SDA: track 318.1 -> 241.7 mm, vias 3 -> 6
- net TEMP_PCB-3: track 2.52 -> 78.3 mm, vias 0 -> 2
- net 3.3V_2: track 393.7 -> 466.7 mm, vias 46 -> 43
- net VBATT_5: track 167.2 -> 96.7 mm, vias 4 -> 5
- net PGND: track 238.4 -> 171.1 mm, vias 9 -> 8
- net !IMU_RESET: track 5.71 -> 63.2 mm, vias 0 -> 5
- net AVDD-0: track 63.8 -> 116.4 mm, vias 7 -> 13
- net TEMP_H-BRIDGE-X: track 9.93 -> 61.6 mm, vias 2 -> 4
- net AGND: track 350.6 -> 402.1 mm, vias 36 -> 37
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- added copper zone on layer 15, net 3.3V_0
- added copper zone on layer 15, net 3.3V_2
- added copper zone on layer 15, net 3.3V_5
- added copper zone on layer 1, net DGND
- added copper zone on layer 16, net DGND
- added copper zone on layer 2, net DGND
- added copper zone on layer 16, net GPS_RFIN
- added copper zone on layer 16, net PGND
- added copper zone on layer 1, net RFGND
- added copper zone on layer 15, net RFGND
- added copper zone on layer 16, net RFGND
- added copper zone on layer 2, net RFGND
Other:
- board text added: "+X"
- board text added: "+Y"
- board text added: "+Z"
- board text added: "-X"
- board text added: "-Y"
- board text added: "-Z"
- board text added: "ADCS"
- board text added: "AVDD-0"
- board text added: "AVDD-1"
- board text added: "Avionics V1.1"
- board text added: "GPS"
- board text added: "IFJR"
- board text added: "IFJR-0"
- board text added: "IFJR-1"
- board text added: "IHU"
- board text added: "IHU-0"
- board text added: "IHU-1"

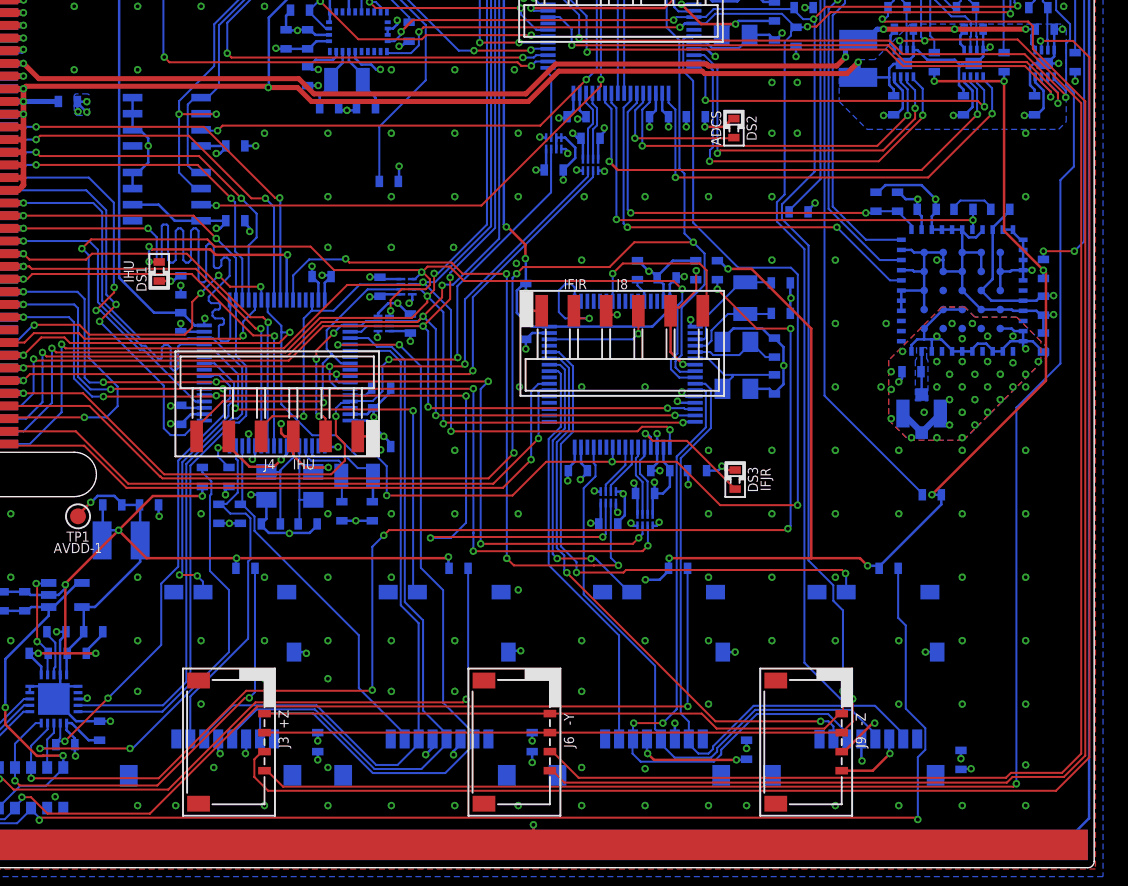
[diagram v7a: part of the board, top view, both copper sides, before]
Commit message: Added signature
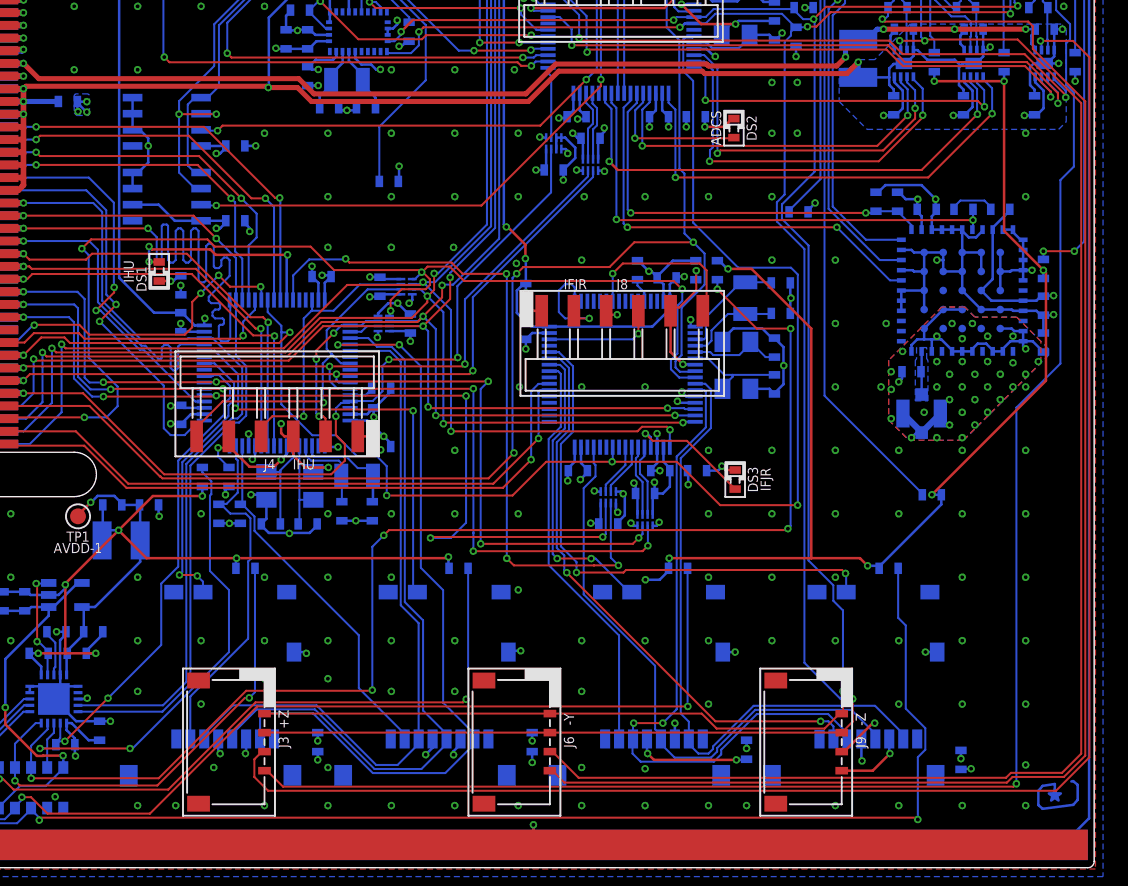
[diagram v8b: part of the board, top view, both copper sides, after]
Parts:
- added LOGO1: SIGNATUREGABE, CougsInSpace-Aesthetics:SIGN-GABE
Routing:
- net DGND: track 1498.7 -> 1507.0 mm
- net PGND: track 171.1 -> 170.4 mm
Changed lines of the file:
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@@
 <grid distance="0.1" unitdist="mm" unit="mm" style="lines" multiple="1" display="yes" altdistance="0.005" altunitdist="mm" altunit="mm"/>
 <layers>
-<layer number="1" name="Top" color="4" fill="1" visible="no" active="yes"/>
-<layer number="2" name="Route2" color="16" fill="10" visible="no" active="yes"/>
+<layer number="1" name="Top" color="4" fill="1" visible="yes" active="yes"/>
+<layer number="2" name="Route2" color="16" fill="10" visible="yes" active="yes"/>
 <layer number="3" name="Route3" color="17" fill="1" visible="no" active="no"/>
 <layer number="4" name="Route4" color="18" fill="1" visible="no" active="no"/>
@@
 <layer number="13" name="Route13" color="21" fill="1" visible="no" active="no"/>
 <layer number="14" name="Route14" color="22" fill="1" visible="no" active="no"/>
-<layer number="15" name="Route15" color="23" fill="1" visible="no" active="yes"/>
+<layer number="15" name="Route15" color="23" fill="1" visible="yes" active="yes"/>
 <layer number="16" name="Bottom" color="1" fill="1" visible="yes" active="yes"/>
 <layer number="17" name="Pads" color="2" fill="1" visible="yes" active="yes"/>
@@
 <layer number="19" name="Unrouted" color="6" fill="1" visible="yes" active="yes"/>
 <layer number="20" name="Dimension" color="24" fill="1" visible="yes" active="yes"/>
-<layer number="21" name="tPlace" color="7" fill="1" visible="no" active="yes"/>
+<layer number="21" name="tPlace" color="7" fill="1" visible="yes" active="yes"/>
 <layer number="22" name="bPlace" color="7" fill="1" visible="yes" active="yes"/>
-<layer number="23" name="tOrigins" color="15" fill="1" visible="no" active="yes"/>
+<layer number="23" name="tOrigins" color="15" fill="1" visible="yes" active="yes"/>
 <layer number="24" name="bOrigins" color="15" fill="1" visible="yes" active="yes"/>
-<layer number="25" name="tNames" color="7" fill="1" visible="no" active="yes"/>
+<layer number="25" name="tNames" color="7" fill="1" visible="yes" active="yes"/>
 <layer number="26" name="bNames" color="7" fill="1" visible="yes" active="yes"/>
 <layer number="27" name="tValues" color="7" fill="1" visible="no" active="yes"/>
@@
 <layer number="37" name="tTest" color="7" fill="1" visible="no" active="yes"/>
 <layer number="38" name="bTest" color="7" fill="1" visible="no" active="yes"/>
-<layer number="39" name="tKeepout" color="4" fill="11" visible="no" active="yes"/>
+<layer number="39" name="tKeepout" color="4" fill="11" visible="yes" active="yes"/>
 <layer number="40" name="bKeepout" color="1" fill="11" visible="yes" active="yes"/>
-<layer number="41" name="tRestrict" color="4" fill="10" visible="no" active="yes"/>
+<layer number="41" name="tRestrict" color="4" fill="10" visible="yes" active="yes"/>
 <layer number="42" name="bRestrict" color="1" fill="10" visible="yes" active="yes"/>
 <layer number="43" name="vRestrict" color="2" fill="10" visible="no" active="yes"/>
@@
 <layer number="49" name="Reference" color="7" fill="1" visible="no" active="yes"/>
 <layer number="50" name="dxf" color="7" fill="1" visible="no" active="no"/>
-<layer number="51" name="tDocu" color="7" fill="1" visible="no" active="yes"/>
-<layer number="52" name="bDocu" color="7" fill="1" visible="no" active="yes"/>
+<layer number="51" name="tDocu" color="7" fill="1" visible="yes" active="yes"/>
+<layer number="52" name="bDocu" color="7" fill="1" visible="yes" active="yes"/>
 <layer number="53" name="tGND_GNDA" color="7" fill="9" visible="no" active="no"/>
 <layer number="54" name="bGND_GNDA" color="1" fill="9" visible="no" active="no"/>
@@
 <attribute name="NAME" x="10.3" y="-21.8" size="0.8" layer="25" font="vector" ratio="15" align="center"/>
 </element>
+<element name="LOGO1" library="CougsInSpace-Aesthetics" package="SIGN-GABE" value="SIGNATUREGABE" x="87.3" y="-42.2" smashed="yes" rot="MR90"/>
 </elements>
 <signals>
@@
 <wire x1="27.07" y1="29.3068125" x2="27.07" y2="20.83769375" width="0.2" layer="16"/>
 <wire x1="27.07" y1="20.83769375" x2="25.34" y2="19.10769375" width="0.2" layer="16"/>
-<wire x1="72.5" y1="14.4" x2="71.8" y2="14.4" width="0.2" layer="16"/>
 <wire x1="6" y1="13.5" x2="6.2" y2="13.7" width="0.4" layer="1"/>
 <wire x1="8.75" y1="12.5" x2="6" y2="12.5" width="0.4" layer="16"/>
@@
 <wire x1="37.895" y1="22.345" x2="37.55" y2="22" width="0.2" layer="16"/>
 <wire x1="14.6" y1="6.905" x2="14.6" y2="5.635" width="0.2" layer="16"/>
-<wire x1="10.25" y1="12.5" x2="10.25" y2="12.6" width="0.2" layer="16"/>
 <wire x1="10.995" y1="12.485" x2="10.265" y2="12.485" width="0.2" layer="16"/>
 <wire x1="10.265" y1="12.485" x2="10.25" y2="12.5" width="0.2" layer="16"/>
@@
 <vertex x="10.1" y="13.1"/>
 </polygon>
+<wire x1="80" y1="-15" x2="75" y2="-15" width="0.2" layer="2"/>
+<wire x1="10" y1="15" x2="10.3" y2="14.7" width="0.2" layer="2"/>
+<wire x1="10.3" y1="14.7" x2="10.3" y2="11.7" width="0.2" layer="2"/>
 </signal>
 <signal name="AGND" class="1">
@@
 <wire x1="85.55" y1="-6.4" x2="86.4" y2="-7.25" width="0.2" layer="16"/>
 <wire x1="84.8" y1="-5.6" x2="84.8" y2="-6.4" width="0.2" layer="16"/>
-<wire x1="78.275" y1="-12.1" x2="78.275" y2="-11.5" width="0.5" layer="16"/>
 <polygon width="0.2" layer="16" thermals="no" rank="2">
 <vertex x="74.2" y="-7.9"/>
@@
 <wire x1="79" y1="-13" x2="80" y2="-12" width="0.2" layer="15"/>
 <wire x1="80" y1="-12" x2="81" y2="-11" width="0.2" layer="15"/>
-<wire x1="81.05" y1="-10.95" x2="82" y2="-10" width="0.2" layer="15"/>
 <wire x1="82" y1="-10" x2="83" y2="-9" width="0.2" layer="15"/>
 <wire x1="83" y1="-9" x2="83.9" y2="-8.1" width="0.2" layer="15"/>
@@
 <vertex x="78.4" y="-3.7"/>
 </polygon>
+<wire x1="81" y1="-11" x2="82" y2="-10" width="0.2" layer="15"/>
+<wire x1="76.8" y1="-13.6" x2="76.4" y2="-13.6" width="0.2" layer="16"/>
+<wire x1="76.4" y1="-13.6" x2="76" y2="-14" width="0.2" layer="16"/>
 </signal>
 <signal name="ADCS_OSC_IN" class="1">
@@
 <mfgpreviewcolor name="substratecolor" color="0xFF786E46"/>
 </mfgpreviewcolors>
+<errors>
+</errors>
 </board>
 </drawing>
